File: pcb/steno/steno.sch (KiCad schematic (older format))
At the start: 58 parts, among them J1 Conn_01x02, K1 KEYSW, K10 KEYSW, K11 KEYSW, K12 KEYSW, K13 KEYSW, K14 KEYSW, K15 KEYSW, K16 KEYSW, K17 KEYSW, K18 KEYSW, K19 KEYSW, K2 KEYSW, K20 KEYSW, K21 KEYSW, K22 KEYSW, K23 KEYSW, K24 KEYSW, K25 KEYSW, K26 KEYSW, K27 KEYSW, K28 KEYSW, K3 KEYSW, K4 KEYSW, K5 KEYSW, K6 KEYSW, K7 KEYSW, K8 KEYSW, K9 KEYSW, U1 Adafruit_Feather

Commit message: Remove v1 files
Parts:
- added D29, D30: DIODE, Diode_THT:D_DO-34_SOD68_P7.62mm_Horizontal, symbol Simulation_SPICE:DIODE
- added J2: Conn_01x04, steno:OLED, symbol Connector_Generic:Conn_01x04
- added K29, K30: KEYSW, Keebio-Parts:Kailh-PG1350-1u-No-Clickhole, symbol canadian_parts:KEYSW
- added U2: MT25QL128ABA1ESE, Package_SO:SOP-8_5.28x5.23mm_P1.27mm, symbol steno:MT25QL128ABA1ESE
- D1, D10, D11, D12, D13, D14, D15, D16, D17, D18, D19, D2, D20, D21, D22, D23, D24, D25, D26, D27, D28, D3, D4, D5, D6, D7, D8, D9: footprint Diode_SMD:D_SOD-123F -> Diode_THT:D_DO-34_SOD68_P7.62mm_Horizontal
- J1: footprint Connector_JST:JST_PH_B2B-PH-SM4-TB_1x02-1MP_P2.00mm_Vertical -> Connector_PinHeader_2.54mm:PinHeader_1x02_P2.54mm_Vertical
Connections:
- net labels added: CS, DQ2, DQ3, MISO_DQ1, MOSI_DQ0, ROW4, ROW5, SCL, SCLK, SDA, VCC
- net labels removed: COL10, COL11, COL7, COL8, COL9
- wire segments 134 -> 119
- no-connect marks 6 -> 4
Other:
- moved on the sheet: D1

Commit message: Update PCB
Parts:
- removed U1: Adafruit_Feather, Downloads:ADAFRUIT_FEATHER, symbol steno-rescue:Adafruit_Feather-ProMicro
- added U1: nice_nano, nice-nano-kicad:nice_nano, symbol nice_nano:nice_nano
- D1, D10, D11, D12, D13, D14, D15, D16, D17, D18, D19, D2, D20, D21, D22, D23, D24, D25, D26, D27, D28, D29, D3, D30, D4, D5, D6, D7, D8, D9: footprint Diode_THT:D_DO-34_SOD68_P7.62mm_Horizontal -> Diode_SMD:D_SOD-123
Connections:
- wire segments 119 -> 25
- no-connect marks 4 -> 0
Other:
- moved on the sheet: U2

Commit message: First PCB version
- Use raw MCU
- Use 5x6 matrix and 30keys (like steno phone)
- Use SOD-123 diodes (like steno phone)
- Use 2.2in TFT for better UX(?)
- Lots of ground plane!
- Add (fake?) logo and contributors
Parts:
- removed J1: Conn_01x02, Connector_PinHeader_2.54mm:PinHeader_1x02_P2.54mm_Vertical, symbol Connector_Generic:Conn_01x02
- removed J2: Conn_01x04, steno:OLED, symbol Connector_Generic:Conn_01x04
- removed K1, K10, K11, K12, K13, K14, K15, K16, K17, K18, K19, K2, K20, K21, K22, K23, K24, K25, K26, K27, K28, K29, K3, K30, K4, K5, K6, K7, K8, K9: KEYSW, Keebio-Parts:Kailh-PG1350-1u-No-Clickhole, symbol canadian_parts:KEYSW
- removed U1: nice_nano, nice-nano-kicad:nice_nano, symbol nice_nano:nice_nano
- added C1, C2: 22pF, Capacitor_SMD:C_0603_1608Metric, symbol Device:C_Small
- added C10, C11, C3, C4, C9: 1uF, Capacitor_SMD:C_0805_2012Metric, symbol Device:C_Small
- added C5, C6, C7: 0.1uF, Capacitor_SMD:C_0603_1608Metric, symbol Device:C_Small
- added C8: 10uF, Capacitor_SMD:C_0805_2012Metric, symbol Device:C_Small
- added F1: Polyfuse_Small, Fuse:Fuse_1206_3216Metric_Castellated, symbol Device:Polyfuse_Small
- added J1: USB_mini_micro_B, Connector_USB:AMPHENOL_10118192-0001LF, symbol keyboard_parts:USB_mini_micro_B
- added K1, K10, K11, K12, K13, K14, K15, K16, K17, K18, K19, K2, K20, K21, K22, K23, K24, K25, K26, K27, K28, K29, K3, K30, K4, K5, K6, K7, K8, K9: SW_Push, Keebio-Parts:Kailh-PG1350-1u-No-Clickhole, symbol Switch:SW_Push
- added R1, R4, R5: 10k, Resistor_SMD:R_0805_2012Metric, symbol Device:R
- added R2, R3: 22, Resistor_SMD:R_0603_1608Metric, symbol Device:R
- added SW1: SW_Push, Button_Switch_SMD:SW_SPST_B3U-1000P, symbol Switch:SW_Push
- added U1: ATmega32U4-AU, Package_QFP:TQFP-44_10x10mm_P0.8mm, symbol MCU_Microchip_ATmega:ATmega32U4-AU
- added U3: MCP1700-3302E_SOT23, Package_TO_SOT_SMD:SOT-23, symbol Regulator_Linear:MCP1700-3302E_SOT23
- added U4: LCD2.2in, steno:LCD2.2in, symbol steno:LCD2.2in
- added Y1: 16MHz, Crystal:Crystal_SMD_EuroQuartz_MJ-4Pin_5.0x3.2mm_HandSoldering, symbol Device:Crystal_GND24_Small
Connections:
- net labels added: +3V3, +5V, C\D, D+, D-, GND1, LCD_CS, LCD_RST, LITE, MISO, MOSI
- net labels removed: BAT, DQ2, DQ3, MISO_DQ1, MOSI_DQ0, RST, SCL, SDA
- wire segments 25 -> 58
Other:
- moved on the sheet: D1, D2, D3, D4, D5, D6, U2

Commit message: [PCB] Final changes
- Add bumper locations on silkscreen
- Add hex buffer for level shifting
- Unify the 2 grounds into 1, removing the decoupling cap
- Add MCU peripheral ref & value to silkscreen
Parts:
- removed C11: 1uF, Capacitor_SMD:C_0805_2012Metric, symbol Device:C_Small
- added U5: 4050, Package_SO:SOIC-16_3.9x9.9mm_P1.27mm, symbol 4xxx:4050
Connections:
- net labels added: CS_3V3, CS_5V, LITE_3V3, LITE_5V, MOSI_3V3, MOSI_5V, SCLK_3V3, SCLK_5V
- net labels removed: CS, GND1, LITE, MOSI, SCLK
- wire segments 58 -> 56
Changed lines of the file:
@@
 ROW2
 Text GLabel 7850 1200 2    50   BiDi ~ 0
-SCLK
+SCLK_5V
 Text GLabel 7850 1300 2    50   BiDi ~ 0
-MOSI
+MOSI_5V
 Text GLabel 7850 1400 2    50   BiDi ~ 0
 MISO
@@
 ROW3
 Text GLabel 6150 3450 2    50   BiDi ~ 0
-MOSI
+MOSI_3V3
 Text GLabel 5200 3250 0    50   BiDi ~ 0
 MISO
 Text GLabel 6150 3350 2    50   BiDi ~ 0
-SCLK
+SCLK_3V3
 Text GLabel 5200 3150 0    50   BiDi ~ 0
-CS
+CS_3V3
 $Comp
 L steno:MT25QL128ABA1ESE U2
@@
 $EndComp
 $Comp
-L power:GND1 #PWR014
-U 1 1 5F7AD817
-P 5200 3450
-F 0 "#PWR014" H 5200 3200 50  0001 C CNN
-F 1 "GND1" V 5205 3322 50  0000 R CNN
-F 2 "" H 5200 3450 50  0001 C CNN
-F 3 "" H 5200 3450 50  0001 C CNN
-	1    5200 3450
-	0    1    1    0
-$EndComp
-$Comp
 L power:GND #PWR020
 U 1 1 5F7B17CE
@@
 	5250 1600 5450 1600
 $Comp
-L power:GND1 #PWR023
-U 1 1 5F7B418E
-P 5000 3850
-F 0 "#PWR023" H 5000 3600 50  0001 C CNN
-F 1 "GND1" H 5005 3677 50  0000 C CNN
-F 2 "" H 5000 3850 50  0001 C CNN
-F 3 "" H 5000 3850 50  0001 C CNN
-	1    5000 3850
-	-1   0    0    1
-$EndComp
-$Comp
 L power:GND #PWR024
 U 1 1 5F79887B
@@
 $EndComp
 $Comp
-L power:PWR_FLAG #FLG03
-U 1 1 5F6F1359
-P 5000 3850
-F 0 "#FLG03" H 5000 3925 50  0001 C CNN
-F 1 "PWR_FLAG" H 5000 4023 50  0000 C CNN
-F 2 "" H 5000 3850 50  0001 C CNN
-F 3 "~" H 5000 3850 50  0001 C CNN
-	1    5000 3850
-	-1   0    0    1
-$EndComp
-$Comp
 L steno:LCD2.2in U4
 U 1 1 5F837536
@@
 	1    0    0    -1
 $EndComp
-Text GLabel 5950 4450 0    50   BiDi ~ 0
-MOSI
 Text GLabel 5950 4550 0    50   BiDi ~ 0
 MISO
-Text GLabel 5950 4650 0    50   BiDi ~ 0
-SCLK
 Text GLabel 5950 4050 0    50   Input ~ 0
 C\D
@@
 LCD_CS
 Text GLabel 5950 4750 0    50   Input ~ 0
-LITE
-$Comp
-L Device:C_Small C11
-U 1 1 5F71423E
-P 5200 3850
-F 0 "C11" V 4971 3850 50  0000 C CNN
-F 1 "1uF" V 5062 3850 50  0000 C CNN
-F 2 "Capacitor_SMD:C_0805_2012Metric" H 5238 3700 50  0001 C CNN
-F 3 "~" H 5200 3850 50  0001 C CNN
-	1    5200 3850
-	0    1    1    0
-$EndComp
-$Comp
-L power:GND1 #PWR015
-U 1 1 5F7A83F2
-P 5950 3850
-F 0 "#PWR015" H 5950 3600 50  0001 C CNN
-F 1 "GND1" H 5955 3677 50  0000 C CNN
-F 2 "" H 5950 3850 50  0001 C CNN
-F 3 "" H 5950 3850 50  0001 C CNN
-	1    5950 3850
-	-1   0    0    1
-$EndComp
+LITE_3V3
 $Comp
 L Device:R R5
@@
 Text GLabel 7850 3900 2    50   Input ~ 0
 LCD_CS
-Wire Wire Line
-	5400 3850 5300 3850
-Connection ~ 5400 3850
-Wire Wire Line
-	5100 3850 5000 3850
-Connection ~ 5000 3850
-$Comp
-L power:+3V3 #PWR017
-U 1 1 5F840B82
-P 5950 3950
-F 0 "#PWR017" H 5950 3800 50  0001 C CNN
-F 1 "+3V3" H 5965 4123 50  0000 C CNN
-F 2 "" H 5950 3950 50  0001 C CNN
-F 3 "" H 5950 3950 50  0001 C CNN
-	1    5950 3950
-	0    -1   -1   0
-$EndComp
 $Comp
 L power:+5V #PWR018
@@
 Text GLabel 7850 3800 2    50   Input ~ 0
 LCD_RST
-Text GLabel 7850 2700 2    50   BiDi ~ 0
+Text GLabel 7850 3000 2    50   BiDi ~ 0
 COL1
-Text GLabel 7850 3000 2    50   BiDi ~ 0
+Text GLabel 7850 1600 2    50   BiDi ~ 0
 COL3
-Text GLabel 7850 2900 2    50   BiDi ~ 0
+Text GLabel 7850 1500 2    50   BiDi ~ 0
 COL2
-Text GLabel 7850 1500 2    50   BiDi ~ 0
+Text GLabel 7850 1700 2    50   BiDi ~ 0
 COL4
-Text GLabel 7850 1700 2    50   BiDi ~ 0
+Text GLabel 7850 2100 2    50   BiDi ~ 0
 COL6
-Text GLabel 7850 1600 2    50   BiDi ~ 0
+Text GLabel 7850 2000 2    50   BiDi ~ 0
 COL5
 Text GLabel 7850 2300 2    50   Input ~ 0
-LITE
-Text GLabel 7850 2000 2    50   BiDi ~ 0
-CS
+LITE_5V
+Text GLabel 7850 2800 2    50   BiDi ~ 0
+CS_5V
+$Comp
+L power:+5V #PWR0101
+U 1 1 5F7617F8
+P 5950 3950
+F 0 "#PWR0101" H 5950 3800 50  0001 C CNN
+F 1 "+5V" H 5965 4123 50  0000 C CNN
+F 2 "" H 5950 3950 50  0001 C CNN
+F 3 "" H 5950 3950 50  0001 C CNN
+	1    5950 3950
+	0    -1   -1   0
+$EndComp
+Text GLabel 9000 2350 0    50   BiDi ~ 0
+CS_5V
+Text GLabel 9000 1400 0    50   BiDi ~ 0
+MOSI_5V
+Text GLabel 9000 1900 0    50   BiDi ~ 0
+SCLK_5V
+Text GLabel 9600 2350 2    50   BiDi ~ 0
+CS_3V3
+Text GLabel 9600 1900 2    50   BiDi ~ 0
+SCLK_3V3
+Text GLabel 9600 1400 2    50   BiDi ~ 0
+MOSI_3V3
+Text GLabel 5950 4650 0    50   BiDi ~ 0
+SCLK_3V3
+Text GLabel 5950 4450 0    50   BiDi ~ 0
+MOSI_3V3
+$Comp
+L power:GND #PWR0108
+U 1 1 5F8C0651
+P 5950 3850
+F 0 "#PWR0108" H 5950 3600 50  0001 C CNN
+F 1 "GND" H 5955 3677 50  0000 C CNN
+F 2 "" H 5950 3850 50  0001 C CNN
+F 3 "" H 5950 3850 50  0001 C CNN
+	1    5950 3850
+	-1   0    0    1
+$EndComp
+$Comp
+L power:GND #PWR0109
+U 1 1 5F8C4316
+P 5200 3450
+F 0 "#PWR0109" H 5200 3200 50  0001 C CNN
+F 1 "GND" H 5205 3277 50  0000 C CNN
+F 2 "" H 5200 3450 50  0001 C CNN
+F 3 "" H 5200 3450 50  0001 C CNN
+	1    5200 3450
+	0    1    1    0
+$EndComp
+$Comp
+L 4xxx:4050 U5
+U 1 1 5F9368CD
+P 9300 1400
+F 0 "U5" H 9300 1717 50  0000 C CNN
+F 1 "4050" H 9300 1626 50  0000 C CNN
+F 2 "Package_SO:SOIC-16_3.9x9.9mm_P1.27mm" H 9300 1400 50  0001 C CNN
+F 3 "http://www.intersil.com/content/dam/intersil/documents/cd40/cd4050bms.pdf" H 9300 1400 50  0001 C CNN
+	1    9300 1400
+	1    0    0    -1
+$EndComp
+$Comp
+L 4xxx:4050 U5
+U 2 1 5F937A2D
+P 9300 1900
+F 0 "U5" H 9300 2217 50  0000 C CNN
+F 1 "4050" H 9300 2126 50  0000 C CNN
+F 2 "Package_SO:SOIC-16_3.9x9.9mm_P1.27mm" H 9300 1900 50  0001 C CNN
+F 3 "http://www.intersil.com/content/dam/intersil/documents/cd40/cd4050bms.pdf" H 9300 1900 50  0001 C CNN
+	2    9300 1900
+	1    0    0    -1
+$EndComp
+$Comp
+L 4xxx:4050 U5
+U 3 1 5F938B9C
+P 9300 2350
+F 0 "U5" H 9300 2667 50  0000 C CNN
+F 1 "4050" H 9300 2576 50  0000 C CNN
+F 2 "Package_SO:SOIC-16_3.9x9.9mm_P1.27mm" H 9300 2350 50  0001 C CNN
+F 3 "http://www.intersil.com/content/dam/intersil/documents/cd40/cd4050bms.pdf" H 9300 2350 50  0001 C CNN
+	3    9300 2350
+	1    0    0    -1
+$EndComp
+$Comp
+L 4xxx:4050 U5
+U 4 1 5F93A4B9
+P 9300 2800
+F 0 "U5" H 9300 3117 50  0000 C CNN
+F 1 "4050" H 9300 3026 50  0000 C CNN
+F 2 "Package_SO:SOIC-16_3.9x9.9mm_P1.27mm" H 9300 2800 50  0001 C CNN
+F 3 "http://www.intersil.com/content/dam/intersil/documents/cd40/cd4050bms.pdf" H 9300 2800 50  0001 C CNN
+	4    9300 2800
+	1    0    0    -1
+$EndComp
+$Comp
+L 4xxx:4050 U5
+U 7 1 5F93BD17
+P 8750 3700
+F 0 "U5" H 8980 3746 50  0000 L CNN
+F 1 "4050" H 8980 3655 50  0000 L CNN
+F 2 "Package_SO:SOIC-16_3.9x9.9mm_P1.27mm" H 8750 3700 50  0001 C CNN
+F 3 "http://www.intersil.com/content/dam/intersil/documents/cd40/cd4050bms.pdf" H 8750 3700 50  0001 C CNN
+	7    8750 3700
+	1    0    0    -1
+$EndComp
+Text GLabel 9000 2800 0    50   Input ~ 0
+LITE_5V
+Text GLabel 9600 2800 2    50   Input ~ 0
+LITE_3V3
+$Comp
+L power:GND #PWR0102
+U 1 1 5F9AA961
+P 8750 4200
+F 0 "#PWR0102" H 8750 3950 50  0001 C CNN
+F 1 "GND" H 8755 4027 50  0000 C CNN
+F 2 "" H 8750 4200 50  0001 C CNN
+F 3 "" H 8750 4200 50  0001 C CNN
+	1    8750 4200
+	1    0    0    -1
+$EndComp
+$Comp
+L power:+3V3 #PWR0103
+U 1 1 5F9ACDB8
+P 8750 3200
+F 0 "#PWR0103" H 8750 3050 50  0001 C CNN
+F 1 "+3V3" H 8765 3373 50  0000 C CNN
+F 2 "" H 8750 3200 50  0001 C CNN
+F 3 "" H 8750 3200 50  0001 C CNN
+	1    8750 3200
+	1    0    0    -1
+$EndComp
 $EndSCHEMATC

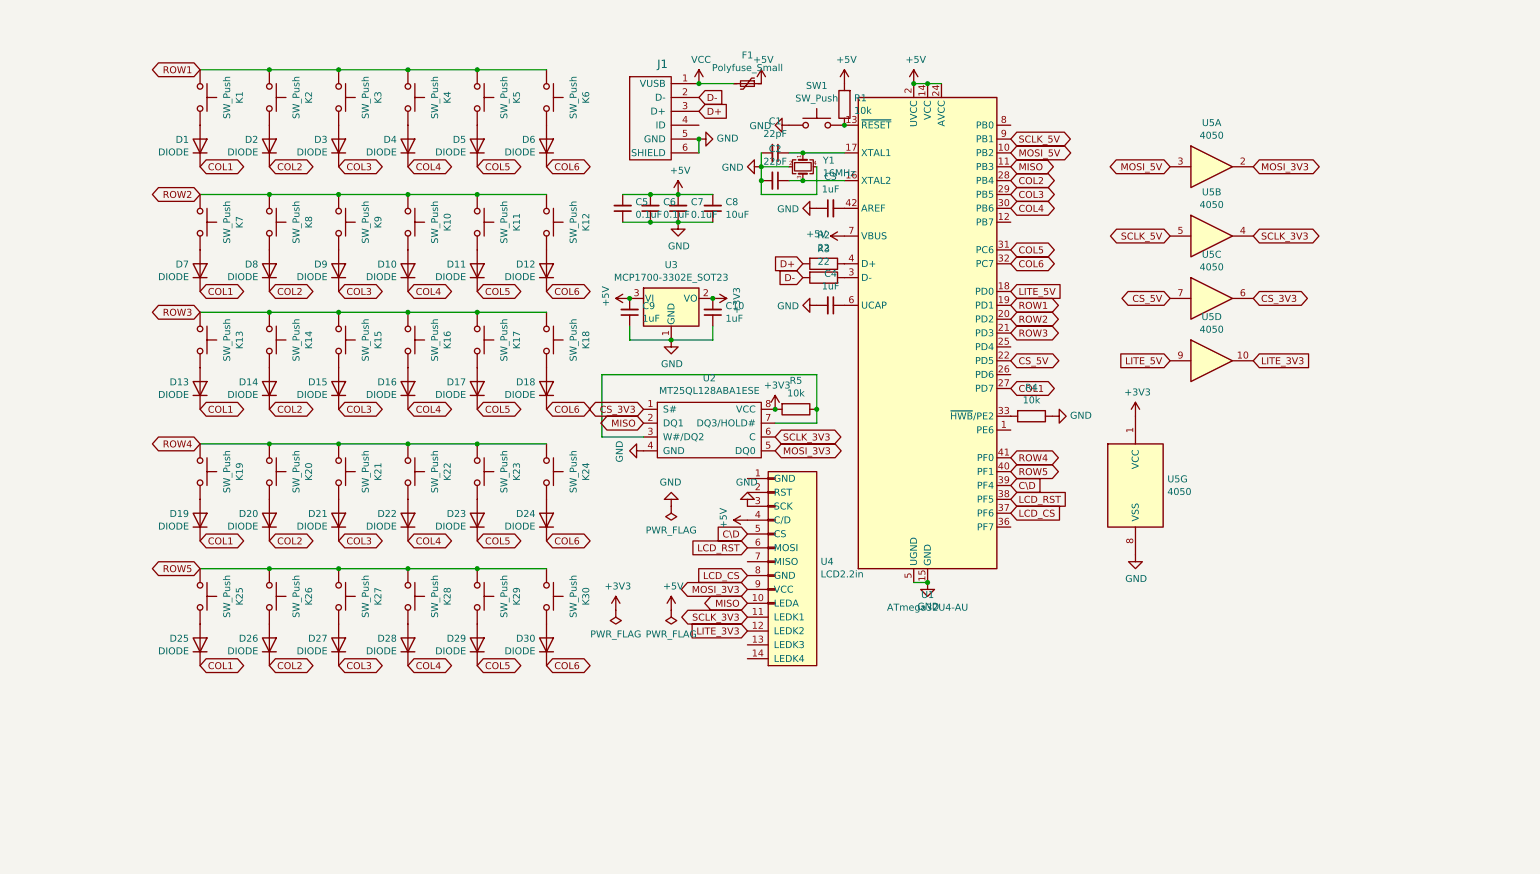
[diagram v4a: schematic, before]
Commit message: [PCB] Use "raw" LCD + backside components
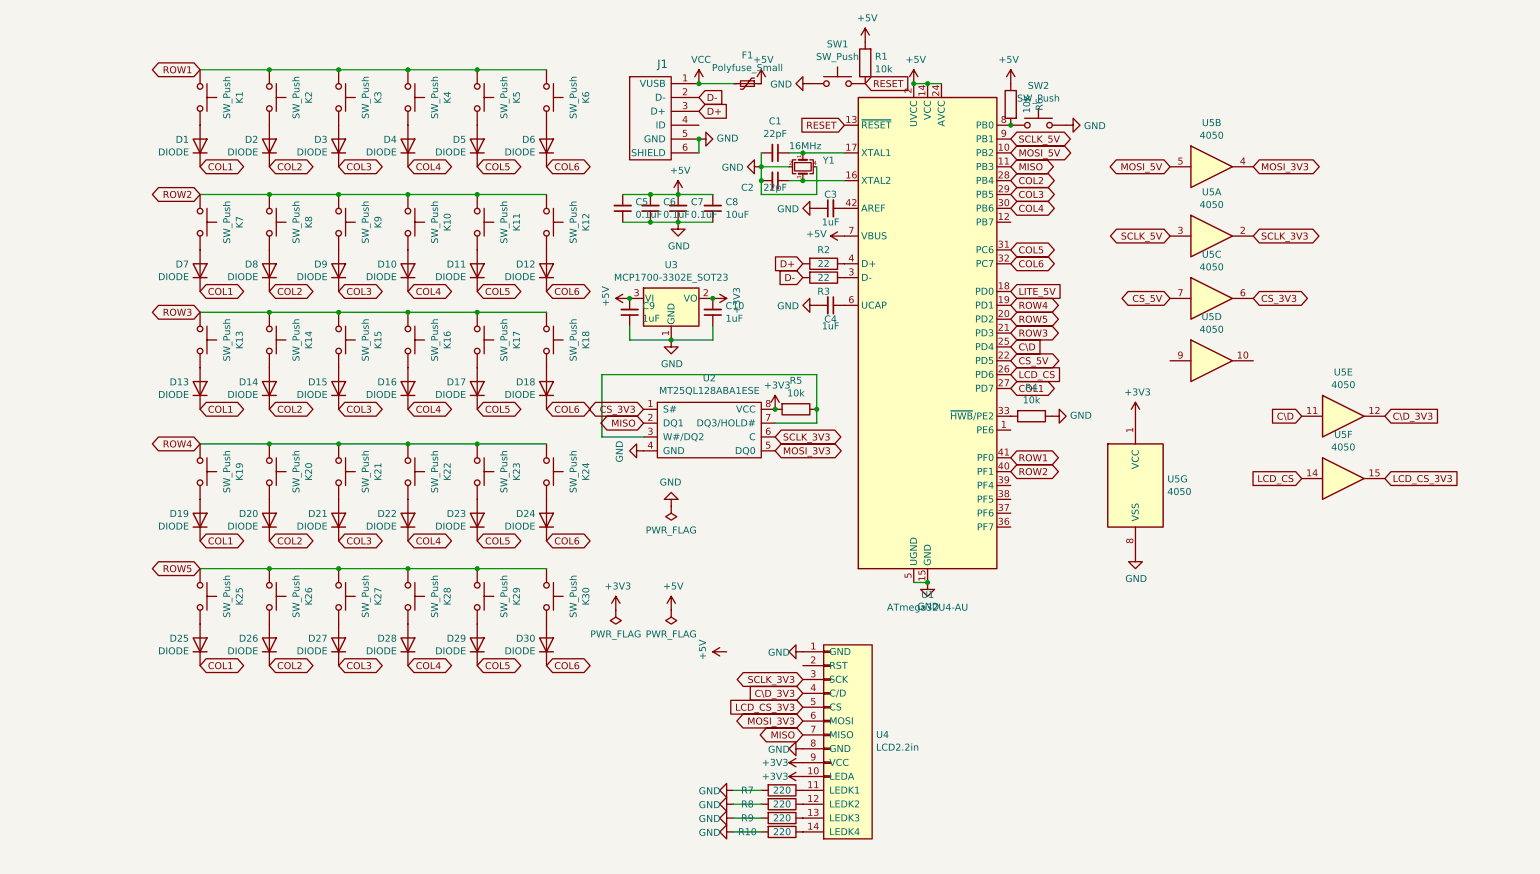
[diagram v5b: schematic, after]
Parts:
- added R10, R7, R8, R9: 220, Resistor_SMD:R_0603_1608Metric, symbol Device:R
- added R6: 10k, Resistor_SMD:R_0805_2012Metric, symbol Device:R
- added SW2: SW_Push, Button_Switch_SMD:SW_SPST_B3U-1000P, symbol Switch:SW_Push
- added unit 5 of U5
- added unit 6 of U5
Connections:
- net +3V3: now also U4.10 (LEDA), U4.9 (VCC)
- net +5V: now also R6.1; no longer U4.4 (C/D)
- net C\D: now also U1.25 (PD4), U5.11; no longer U1.39 (PF4), U4.5 (CS)
- net GND: now also U4.1 (GND), U4.8 (GND), R10.2, R7.2, R8.2, R9.2, SW2.1; no longer U4.3 (SCK)
- net LCD_CS: now also U1.26 (PD6), U5.14; no longer U1.37 (PF6), U4.8 (GND)
- net LITE_5V: no longer U5.9
- net MISO: now also U4.7 (MISO); no longer U4.10 (LEDA)
- net MOSI_3V3: now also U4.6 (MOSI), U5.4; no longer U4.9 (VCC), U5.2
- net MOSI_5V: now also U5.5; no longer U5.3
- net ROW1: now also U1.41 (PF0); no longer U1.19 (PD1)
- net ROW2: now also U1.40 (PF1); no longer U1.20 (PD2)
- net ROW4: now also U1.19 (PD1); no longer U1.41 (PF0)
- net ROW5: now also U1.20 (PD2); no longer U1.40 (PF1)
- net SCLK_3V3: now also U4.3 (SCK), U5.2; no longer U4.11 (LEDK1), U5.4
- net SCLK_5V: now also U5.3; no longer U5.5
- net RESET: now reaches R1.1, SW1.2, U1.13 (~RESET)
- net at U1.8 (PB0): now also R6.2, SW2.2
- net at U4.13 (LEDK3): now also R9.1
- net at U4.14 (LEDK4): now also R10.1
- net LCD_RST: no longer names the net of U1.38 (PF5)
- net LCD_RST: no longer U4.6 (MOSI)
- net LITE_3V3: no longer names the net of U4.12 (LEDK2)
- net LITE_3V3: now also R8.1; no longer U5.10
- new net: R7.1, U4.11 (LEDK1)
- new net C\D_3V3: U4.4 (C/D), U5.12
- new net LCD_CS_3V3: U4.5 (CS), U5.15
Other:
- moved on the sheet: R1, SW1, U4, U5A, U5B

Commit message: [PCB] Use new PG1350 footprint + remove unneeded libraries
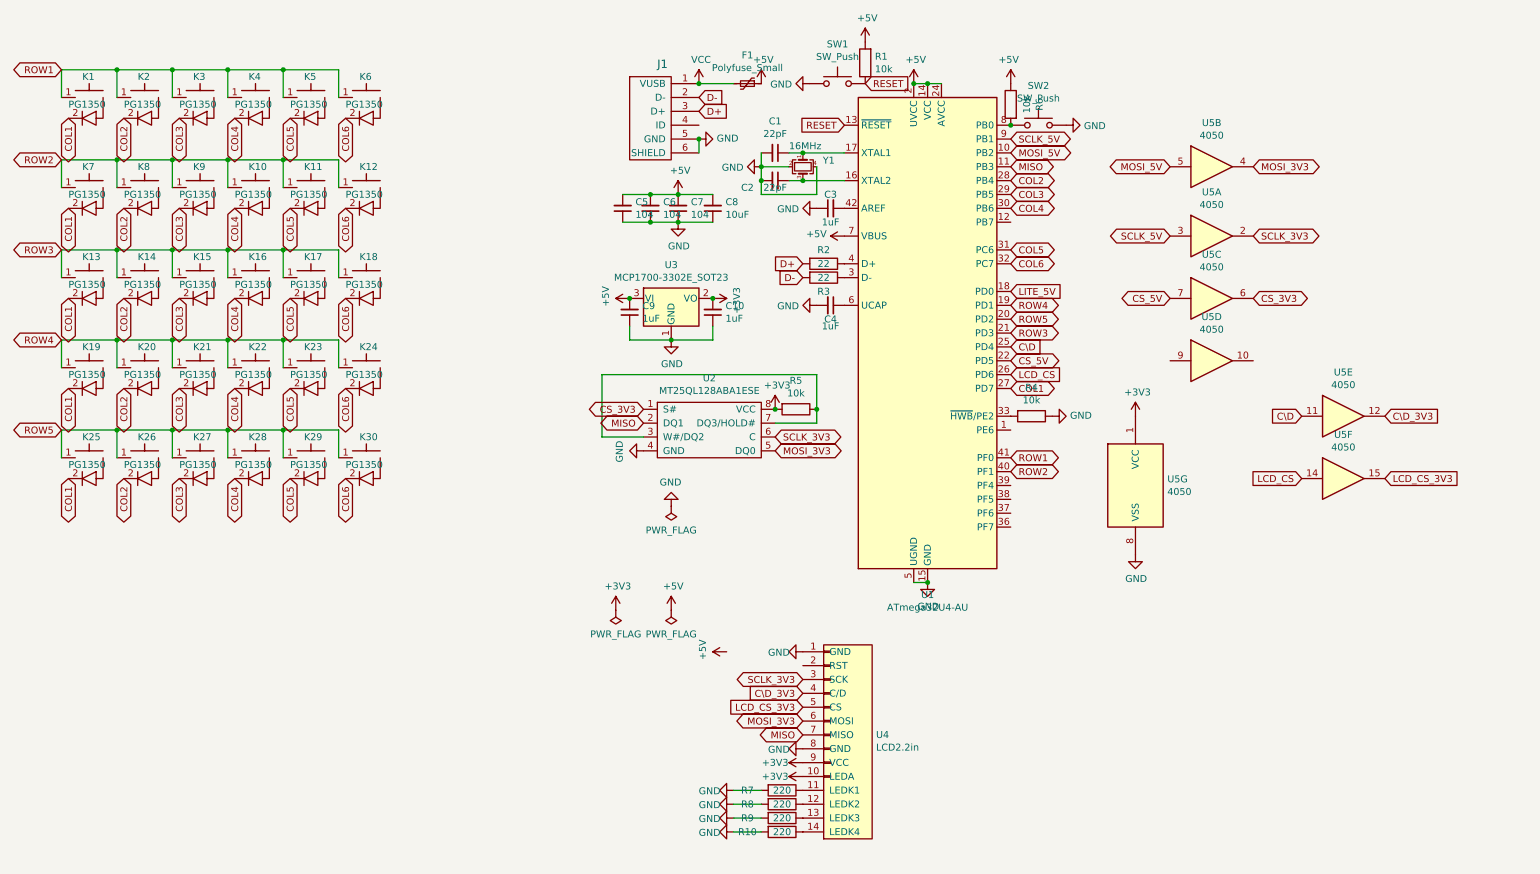
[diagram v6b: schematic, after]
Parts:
- removed D1, D10, D11, D12, D13, D14, D15, D16, D17, D18, D19, D2, D20, D21, D22, D23, D24, D25, D26, D27, D28, D29, D3, D30, D4, D5, D6, D7, D8, D9: DIODE, Diode_SMD:D_SOD-123, symbol Simulation_SPICE:DIODE
- removed K1, K10, K11, K12, K13, K14, K15, K16, K17, K18, K19, K2, K20, K21, K22, K23, K24, K25, K26, K27, K28, K29, K3, K30, K4, K5, K6, K7, K8, K9: SW_Push, Keebio-Parts:Kailh-PG1350-1u-No-Clickhole, symbol Switch:SW_Push
- added K1, K10, K11, K12, K13, K14, K15, K16, K17, K18, K19, K2, K20, K21, K22, K23, K24, K25, K26, K27, K28, K29, K3, K30, K4, K5, K6, K7, K8, K9: PG1350, pg1350:PG1350, symbol pg1350:PG1350
- C5, C6, C7: value 0.1uF -> 104
- Y1: footprint Crystal:Crystal_SMD_EuroQuartz_MJ-4Pin_5.0x3.2mm_HandSoldering -> Crystal:Crystal_SMD_EuroQuartz_MJ-4Pin_5.0x3.2mm
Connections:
- net COL1: now also K1.2, K13.2, K19.2, K25.2, K7.2
- net COL2: now also K14.2, K2.2, K20.2, K26.2, K8.2
- net COL3: now also K15.2, K21.2, K27.2, K3.2, K9.2
- net COL4: now also K10.2, K16.2, K22.2, K28.2, K4.2
- net COL5: now also K11.2, K17.2, K23.2, K29.2, K5.2
- net COL6: now also K12.2, K18.2, K24.2, K30.2, K6.2
- net ROW1: now also K1.1, K2.1, K3.1, K4.1, K5.1, K6.1
- net ROW2: now also K10.1, K11.1, K12.1, K7.1, K8.1, K9.1
- net ROW3: now also K13.1, K14.1, K15.1, K16.1, K17.1, K18.1
- net ROW4: now also K19.1, K20.1, K21.1, K22.1, K23.1, K24.1
- net ROW5: now also K25.1, K26.1, K27.1, K28.1, K29.1, K30.1
